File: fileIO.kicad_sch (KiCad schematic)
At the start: 26 parts, among them J3 USB_C, J5 Conn_02x03_Odd_Even, J7 M20-7920642R, SW1 SW_Push

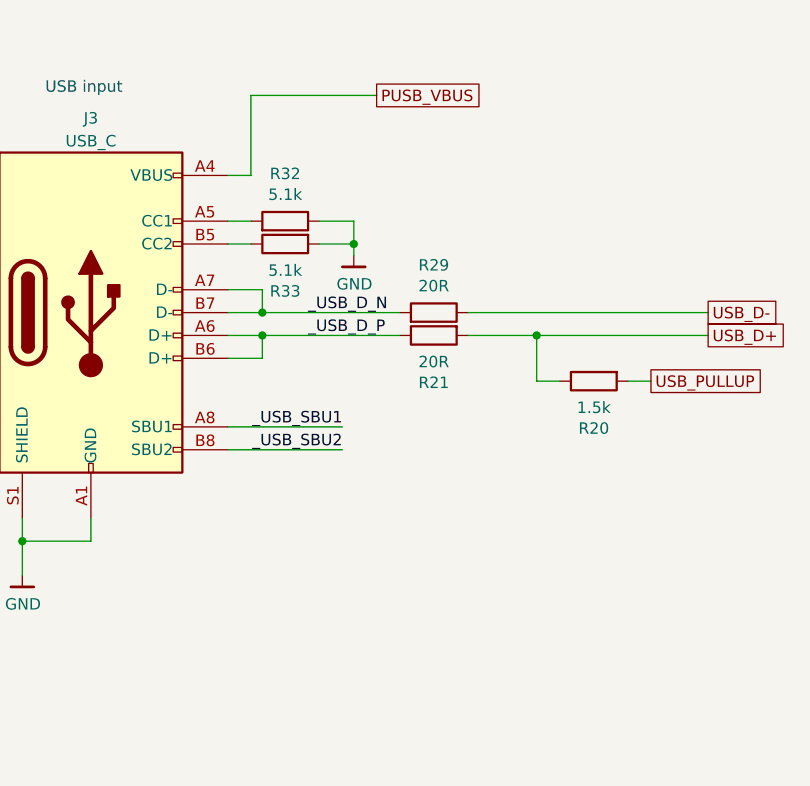
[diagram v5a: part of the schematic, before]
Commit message: Add USB-C power management chip
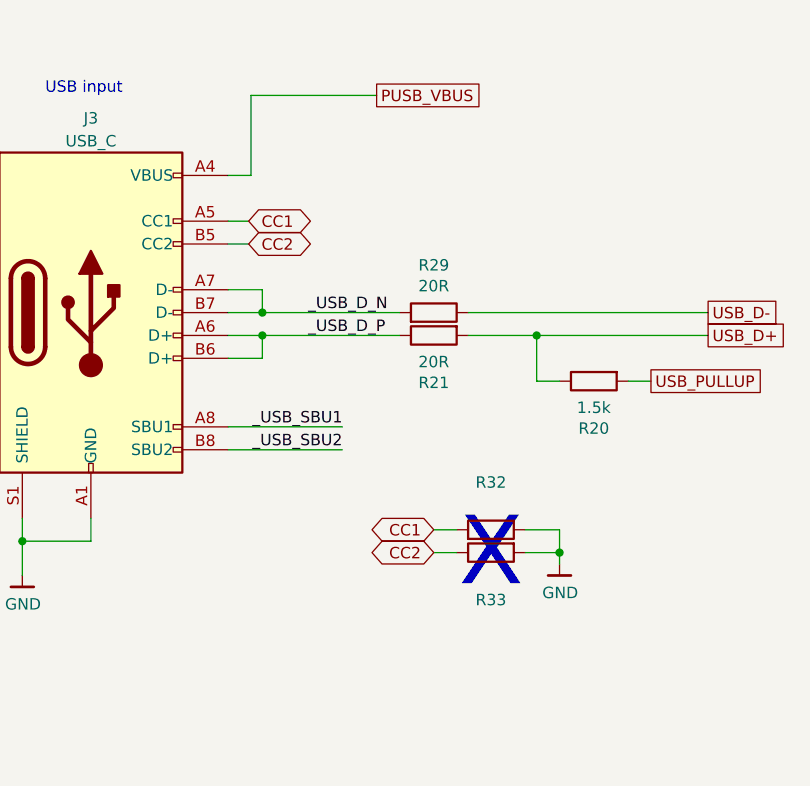
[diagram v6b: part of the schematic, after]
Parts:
- R32: value 5.1k -> (none); footprint Resistor_SMD:R_0201_0603Metric -> (none); Mfg ‎Yageo‎ -> ‎Yageo; now left out of the parts list
- R33: value 5.1k -> (none); footprint Resistor_SMD:R_0201_0603Metric -> (none); Mfg ‎Yageo‎ -> Yageo; now left out of the parts list
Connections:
- net CC1: now reaches J3.A5 (CC1), R32.2
- net CC2: now reaches J3.B5 (CC2), R33.1
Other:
- note added: "X"
- moved on the sheet: R32, R33
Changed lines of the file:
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@@
   (junction (at 57.15 80.01) (diameter 0) (color 0 0 0 0)
   )
-  (junction (at 67.31 69.85) (diameter 0) (color 0 0 0 0)
+  (junction (at 90.17 104.14) (diameter 0) (color 0 0 0 0)
   )
   (junction (at 183.515 135.89) (diameter 0) (color 0 0 0 0)
@@
     (stroke (width 0) (type default) (color 0 0 0 0))
   )
+  (wire (pts (xy 53.34 69.85) (xy 55.626 69.85))
+    (stroke (width 0) (type default) (color 0 0 0 0))
+  )
   (wire (pts (xy 170.815 109.22) (xy 170.815 124.46))
     (stroke (width 0) (type default) (color 0 0 0 0))
@@
     (stroke (width 0) (type default) (color 0 0 0 0))
   )
-  (wire (pts (xy 53.34 67.31) (xy 55.88 67.31))
+  (wire (pts (xy 76.2 101.6) (xy 78.74 101.6))
     (stroke (width 0) (type default) (color 0 0 0 0))
   )
@@
     (stroke (width 0) (type default) (color 0 0 0 0))
   )
-  (wire (pts (xy 67.31 69.85) (xy 67.31 71.12))
+  (wire (pts (xy 90.17 104.14) (xy 90.17 105.41))
     (stroke (width 0) (type default) (color 0 0 0 0))
   )
@@
     (stroke (width 0) (type default) (color 0 0 0 0))
   )
-  (wire (pts (xy 63.5 69.85) (xy 67.31 69.85))
-    (stroke (width 0) (type default) (color 0 0 0 0))
-  )
-  (wire (pts (xy 63.5 67.31) (xy 67.31 67.31))
+  (wire (pts (xy 86.36 104.14) (xy 90.17 104.14))
+    (stroke (width 0) (type default) (color 0 0 0 0))
+  )
+  (wire (pts (xy 86.36 101.6) (xy 90.17 101.6))
     (stroke (width 0) (type default) (color 0 0 0 0))
   )
@@
     (stroke (width 0) (type default) (color 0 0 0 0))
   )
-  (wire (pts (xy 53.34 69.85) (xy 55.88 69.85))
+  (wire (pts (xy 76.2 104.14) (xy 78.74 104.14))
     (stroke (width 0) (type default) (color 0 0 0 0))
   )
@@
     (stroke (width 0) (type default) (color 0 0 0 0))
   )
+  (wire (pts (xy 53.34 67.31) (xy 55.626 67.31))
+    (stroke (width 0) (type default) (color 0 0 0 0))
+  )
   (wire (pts (xy 223.52 130.81) (xy 223.52 138.43))
     (stroke (width 0) (type default) (color 0 0 0 0))
@@
     (stroke (width 0) (type default) (color 0 0 0 0))
   )
-  (wire (pts (xy 67.31 67.31) (xy 67.31 69.85))
+  (wire (pts (xy 90.17 101.6) (xy 90.17 104.14))
     (stroke (width 0) (type default) (color 0 0 0 0))
   )
@@
   (wire (pts (xy 53.34 62.23) (xy 55.88 62.23))
     (stroke (width 0) (type default) (color 0 0 0 0))
+  )
+  (text "X" (at 78.994 108.712 0)
+    (effects (font (size 7.62 7.62)) (justify left bottom))
   )
   (text "Dual Pmod" (at 217.17 105.41 0)
@@
     )
   )
+  (global_label "CC1" (shape bidirectional) (at 55.626 67.31 0) (fields_autoplaced)
+    (effects (font (size 1.27 1.27)) (justify left))
+    (property "Intersheet References" "${INTERSHEET_REFS}" (id 0) (at 61.6997 67.2306 0)
+      (effects (font (size 1.27 1.27)) (justify left) hide)
+    )
+  )
   (global_label "LED_B" (shape passive) (at 205.74 39.37 180) (fields_autoplaced)
     (effects (font (size 1.27 1.27)) (justify right))
@@
     )
   )
+  (global_label "CC2" (shape bidirectional) (at 76.2 104.14 180) (fields_autoplaced)
+    (effects (font (size 1.27 1.27)) (justify right))
+    (property "Intersheet References" "${INTERSHEET_REFS}" (id 0) (at 70.1263 104.0606 0)
+      (effects (font (size 1.27 1.27)) (justify right) hide)
+    )
+  )
   (global_label "PMOD3" (shape input) (at 213.36 86.36 180) (fields_autoplaced)
     (effects (font (size 1.27 1.27)) (justify right))
@@
     (property "Intersheet References" "${INTERSHEET_REFS}" (id 0) (at 0 0 0)
       (effects (font (size 1.27 1.27)) hide)
+    )
+  )
+  (global_label "CC1" (shape bidirectional) (at 76.2 101.6 180) (fields_autoplaced)
+    (effects (font (size 1.27 1.27)) (justify right))
+    (property "Intersheet References" "${INTERSHEET_REFS}" (id 0) (at 70.1263 101.6794 0)
+      (effects (font (size 1.27 1.27)) (justify right) hide)
     )
   )
@@
     (effects (font (size 1.27 1.27)) (justify left))
     (property "Intersheet References" "${INTERSHEET_REFS}" (id 0) (at 265.3956 125.6506 0)
+      (effects (font (size 1.27 1.27)) (justify left) hide)
+    )
+  )
+  (global_label "CC2" (shape bidirectional) (at 55.626 69.85 0) (fields_autoplaced)
+    (effects (font (size 1.27 1.27)) (justify left))
+    (property "Intersheet References" "${INTERSHEET_REFS}" (id 0) (at 61.6997 69.7706 0)
       (effects (font (size 1.27 1.27)) (justify left) hide)
     )
@@
     (pin "1")
   )
-  (symbol (lib_id "Device:R") (at 59.69 67.31 270) (mirror x) (unit 1)
-    (in_bom yes) (on_board yes)
-    (property "Reference" "R32" (id 0) (at 59.69 62.0522 90))
-    (property "Value" "5.1k" (id 1) (at 59.69 64.3636 90))
-    (property "Footprint" "Resistor_SMD:R_0201_0603Metric" (id 2) (at 59.69 69.088 90)
-      (effects (font (size 1.27 1.27)) hide)
-    )
-    (property "Datasheet" "~" (id 3) (at 59.69 67.31 0)
-      (effects (font (size 1.27 1.27)) hide)
-    )
-    (property "Mfg" "‎Yageo‎" (id 4) (at 59.69 67.31 0)
-      (effects (font (size 1.27 1.27)) hide)
-    )
-    (property "PN" "RC0201JR-075K1L" (id 5) (at 59.69 67.31 0)
-      (effects (font (size 1.27 1.27)) hide)
-    )
-    (property "Mouser Part No" "603-RC0201JR-075K1L" (id 6) (at 59.69 67.31 0)
-      (effects (font (size 1.27 1.27)) hide)
-    )
-    (property "Pricing (EUR)" "0,10" (id 7) (at 59.69 67.31 0)
+  (symbol (lib_id "Device:R") (at 82.55 101.6 270) (mirror x) (unit 1)
+    (in_bom no) (on_board yes)
+    (property "Reference" "R32" (id 0) (at 82.55 96.3422 90))
+    (property "Value" "" (id 1) (at 82.55 98.6536 90))
+    (property "Footprint" "" (id 2) (at 82.55 103.378 90)
+      (effects (font (size 1.27 1.27)) hide)
+    )
+    (property "Datasheet" "~" (id 3) (at 82.55 101.6 0)
+      (effects (font (size 1.27 1.27)) hide)
+    )
+    (property "Mfg" "‎Yageo" (id 4) (at 82.55 101.6 0)
+      (effects (font (size 1.27 1.27)) hide)
+    )
+    (property "PN" "RC0201JR-075K1L" (id 5) (at 82.55 101.6 0)
+      (effects (font (size 1.27 1.27)) hide)
+    )
+    (property "Mouser Part No" "603-RC0201JR-075K1L" (id 6) (at 82.55 101.6 0)
+      (effects (font (size 1.27 1.27)) hide)
+    )
+    (property "Pricing (EUR)" "0,10" (id 7) (at 82.55 101.6 0)
       (effects (font (size 1.27 1.27)) hide)
     )
@@
     (pin "2")
   )
-  (symbol (lib_id "Device:R") (at 59.69 69.85 90) (mirror x) (unit 1)
-    (in_bom yes) (on_board yes)
-    (property "Reference" "R33" (id 0) (at 59.69 75.1078 90))
-    (property "Value" "5.1k" (id 1) (at 59.69 72.7964 90))
-    (property "Footprint" "Resistor_SMD:R_0201_0603Metric" (id 2) (at 59.69 68.072 90)
-      (effects (font (size 1.27 1.27)) hide)
-    )
-    (property "Datasheet" "~" (id 3) (at 59.69 69.85 0)
-      (effects (font (size 1.27 1.27)) hide)
-    )
-    (property "Mfg" "‎Yageo‎" (id 4) (at 59.69 69.85 0)
-      (effects (font (size 1.27 1.27)) hide)
-    )
-    (property "PN" "RC0201JR-075K1L" (id 5) (at 59.69 69.85 0)
-      (effects (font (size 1.27 1.27)) hide)
-    )
-    (property "Mouser Part No" "603-RC0201JR-075K1L" (id 6) (at 59.69 69.85 0)
-      (effects (font (size 1.27 1.27)) hide)
-    )
-    (property "Pricing (EUR)" "0,10" (id 7) (at 59.69 69.85 0)
+  (symbol (lib_id "Device:R") (at 82.55 104.14 90) (mirror x) (unit 1)
+    (in_bom no) (on_board yes)
+    (property "Reference" "R33" (id 0) (at 82.55 109.3978 90))
+    (property "Value" "" (id 1) (at 82.55 107.0864 90))
+    (property "Footprint" "" (id 2) (at 82.55 102.362 90)
+      (effects (font (size 1.27 1.27)) hide)
+    )
+    (property "Datasheet" "~" (id 3) (at 82.55 104.14 0)
+      (effects (font (size 1.27 1.27)) hide)
+    )
+    (property "Mfg" "Yageo" (id 4) (at 82.55 104.14 0)
+      (effects (font (size 1.27 1.27)) hide)
+    )
+    (property "PN" "RC0201JR-075K1L" (id 5) (at 82.55 104.14 0)
+      (effects (font (size 1.27 1.27)) hide)
+    )
+    (property "Mouser Part No" "603-RC0201JR-075K1L" (id 6) (at 82.55 104.14 0)
+      (effects (font (size 1.27 1.27)) hide)
+    )
+    (property "Pricing (EUR)" "0,10" (id 7) (at 82.55 104.14 0)
       (effects (font (size 1.27 1.27)) hide)
     )
@@
     (pin "2")
   )
-  (symbol (lib_id "gkl_power:GND") (at 67.31 71.12 0) (unit 1)
-    (in_bom yes) (on_board yes)
-    (property "Reference" "#PWR06" (id 0) (at 67.31 77.47 0)
-      (effects (font (size 1.27 1.27)) hide)
-    )
-    (property "Value" "GND" (id 1) (at 67.3862 74.3204 0))
-    (property "Footprint" "" (id 2) (at 64.77 80.01 0)
-      (effects (font (size 1.27 1.27)) hide)
-    )
-    (property "Datasheet" "" (id 3) (at 67.31 71.12 0)
-      (effects (font (size 1.27 1.27)) hide)
-    )
+  (symbol (lib_id "gkl_power:GND") (at 90.17 105.41 0) (unit 1)
+    (in_bom yes) (on_board yes)
+    (property "Reference" "#PWR06" (id 0) (at 90.17 111.76 0)
+      (effects (font (size 1.27 1.27)) hide)
+    )
+    (property "Value" "GND" (id 1) (at 90.2462 108.6104 0))
+    (property "Footprint" "" (id 2) (at 87.63 114.3 0)
+      (effects (font (size 1.27 1.27)) hide)
+    )
+    (property "Datasheet" "" (id 3) (at 90.17 105.41 0)
+      (effects (font (size 1.27 1.27)) hide)
+    )

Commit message: Convert to KiCAD 7
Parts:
- R32, R33: value (none) -> 5.1k; footprint (none) -> Resistor_SMD:R_0201_0603Metric

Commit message: Update component prices
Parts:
- C76: Pricing (EUR) 0,09 -> 0,08
- D1: Pricing (EUR) 2,03 -> 1,73
- D4: Pricing (EUR) 0,41 -> 0,36
- J3: Pricing (EUR) 0,77 -> 0,75
- J7: Pricing (EUR) 1,99 -> 1,97
- R20: Pricing (EUR) 0,11 -> 0,09
- R21, R22, R23, R24, R29, R33, R4: Pricing (EUR) 0,10 -> 0,09
- R32: Mfg ‎Yageo -> Yageo; Pricing (EUR) 0,10 -> 0,09
- RN2: Pricing (EUR) 0,31 -> 0,27
- SW1: Pricing (EUR) 5,11 -> 3,45
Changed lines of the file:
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@@
       (effects (font (size 1.27 1.27)) hide)
     )
-    (property "Pricing (EUR)" "0,77" (at 38.1 77.47 0)
+    (property "Pricing (EUR)" "0,75" (at 38.1 77.47 0)
       (effects (font (size 1.27 1.27)) hide)
     )
@@
       (effects (font (size 1.27 1.27)) hide)
     )
-    (property "Pricing (EUR)" "0,11" (at 93.98 85.09 0)
+    (property "Pricing (EUR)" "0,09" (at 93.98 85.09 0)
       (effects (font (size 1.27 1.27)) hide)
     )
@@
       (effects (font (size 1.27 1.27)) hide)
     )
-    (property "Pricing (EUR)" "0,10" (at 214.63 29.21 0)
+    (property "Pricing (EUR)" "0,09" (at 214.63 29.21 0)
       (effects (font (size 1.27 1.27)) hide)
     )
@@
       (effects (font (size 1.27 1.27)) hide)
     )
-    (property "Pricing (EUR)" "0,10" (at 214.63 34.29 0)
+    (property "Pricing (EUR)" "0,09" (at 214.63 34.29 0)
       (effects (font (size 1.27 1.27)) hide)
     )
@@
       (effects (font (size 1.27 1.27)) hide)
     )
-    (property "Pricing (EUR)" "5,11" (at 133.35 44.45 0)
+    (property "Pricing (EUR)" "3,45" (at 133.35 44.45 0)
       (effects (font (size 1.27 1.27)) hide)
     )
@@
       (effects (font (size 1.27 1.27)) hide)
     )
-    (property "Pricing (EUR)" "0,10" (at 144.78 38.1 0)
+    (property "Pricing (EUR)" "0,09" (at 144.78 38.1 0)
       (effects (font (size 1.27 1.27)) hide)
     )
@@
       (effects (font (size 1.27 1.27)) hide)
     )
-    (property "Pricing (EUR)" "0,09" (at 148.59 49.53 0)
+    (property "Pricing (EUR)" "0,08" (at 148.59 49.53 0)
       (effects (font (size 1.27 1.27)) hide)
     )
@@
       (effects (font (size 1.27 1.27)) hide)
     )
-    (property "Pricing (EUR)" "0,10" (at 76.2 80.01 0)
+    (property "Pricing (EUR)" "0,09" (at 76.2 80.01 0)
       (effects (font (size 1.27 1.27)) hide)
     )
@@
       (effects (font (size 1.27 1.27)) hide)
     )
-    (property "Pricing (EUR)" "0,10" (at 76.2 77.47 0)
+    (property "Pricing (EUR)" "0,09" (at 76.2 77.47 0)
       (effects (font (size 1.27 1.27)) hide)
     )
@@
       (effects (font (size 1.27 1.27)) hide)
     )
-    (property "Pricing (EUR)" "0,10" (at 214.63 39.37 0)
+    (property "Pricing (EUR)" "0,09" (at 214.63 39.37 0)
       (effects (font (size 1.27 1.27)) hide)
     )
@@
       (effects (font (size 1.27 1.27)) hide)
     )
-    (property "Pricing (EUR)" "2,03" (at 226.06 34.29 0)
+    (property "Pricing (EUR)" "1,73" (at 226.06 34.29 0)
       (effects (font (size 1.27 1.27)) hide)
     )
@@
       (effects (font (size 1.27 1.27)) hide)
     )
-    (property "Mfg" "‎Yageo" (at 82.55 101.6 0)
+    (property "Mfg" "Yageo" (at 82.55 101.6 0)
       (effects (font (size 1.27 1.27)) hide)
     )
@@
       (effects (font (size 1.27 1.27)) hide)
     )
-    (property "Pricing (EUR)" "0,10" (at 82.55 101.6 0)
+    (property "Pricing (EUR)" "0,09" (at 82.55 101.6 0)
       (effects (font (size 1.27 1.27)) hide)
     )
@@
       (effects (font (size 1.27 1.27)) hide)
     )
-    (property "Pricing (EUR)" "0,10" (at 82.55 104.14 0)
+    (property "Pricing (EUR)" "0,09" (at 82.55 104.14 0)
       (effects (font (size 1.27 1.27)) hide)
     )
@@
       (effects (font (size 1.27 1.27)) hide)
     )
-    (property "Pricing (EUR)" "0,41" (at 223.52 146.05 0)
+    (property "Pricing (EUR)" "0,36" (at 223.52 146.05 0)
       (effects (font (size 1.27 1.27)) hide)
     )
@@
       (effects (font (size 1.27 1.27)) hide)
     )
-    (property "Pricing (EUR)" "1,99" (at 182.245 124.46 0)
+    (property "Pricing (EUR)" "1,97" (at 182.245 124.46 0)
       (effects (font (size 1.27 1.27)) hide)
     )
@@
       (effects (font (size 1.27 1.27)) hide)
     )
-    (property "Pricing (EUR)" "0,31" (at 246.38 123.19 0)
-      (effects (font (size 1.27 1.27)) hide)
-    )
+    (property "Pricing (EUR)" "0,27" (at 246.38 123.19 0)
+      (effects (font (size 1.27 1.27)) hide)
+    )
